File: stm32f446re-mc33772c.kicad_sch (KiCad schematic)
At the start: 44 parts, among them J1 Conn_01x02, J2 USB_B_Micro, J3 Conn_01x03, J4 Conn_01x06, J6 SM06B-GHS-TB, U1 STM32F446RETx, U3 LD1086D2M33TR, U4 AMS1117-3.3, U6 LMR51450SDRRR, U7 SN65HVD232, Y1 16MHz

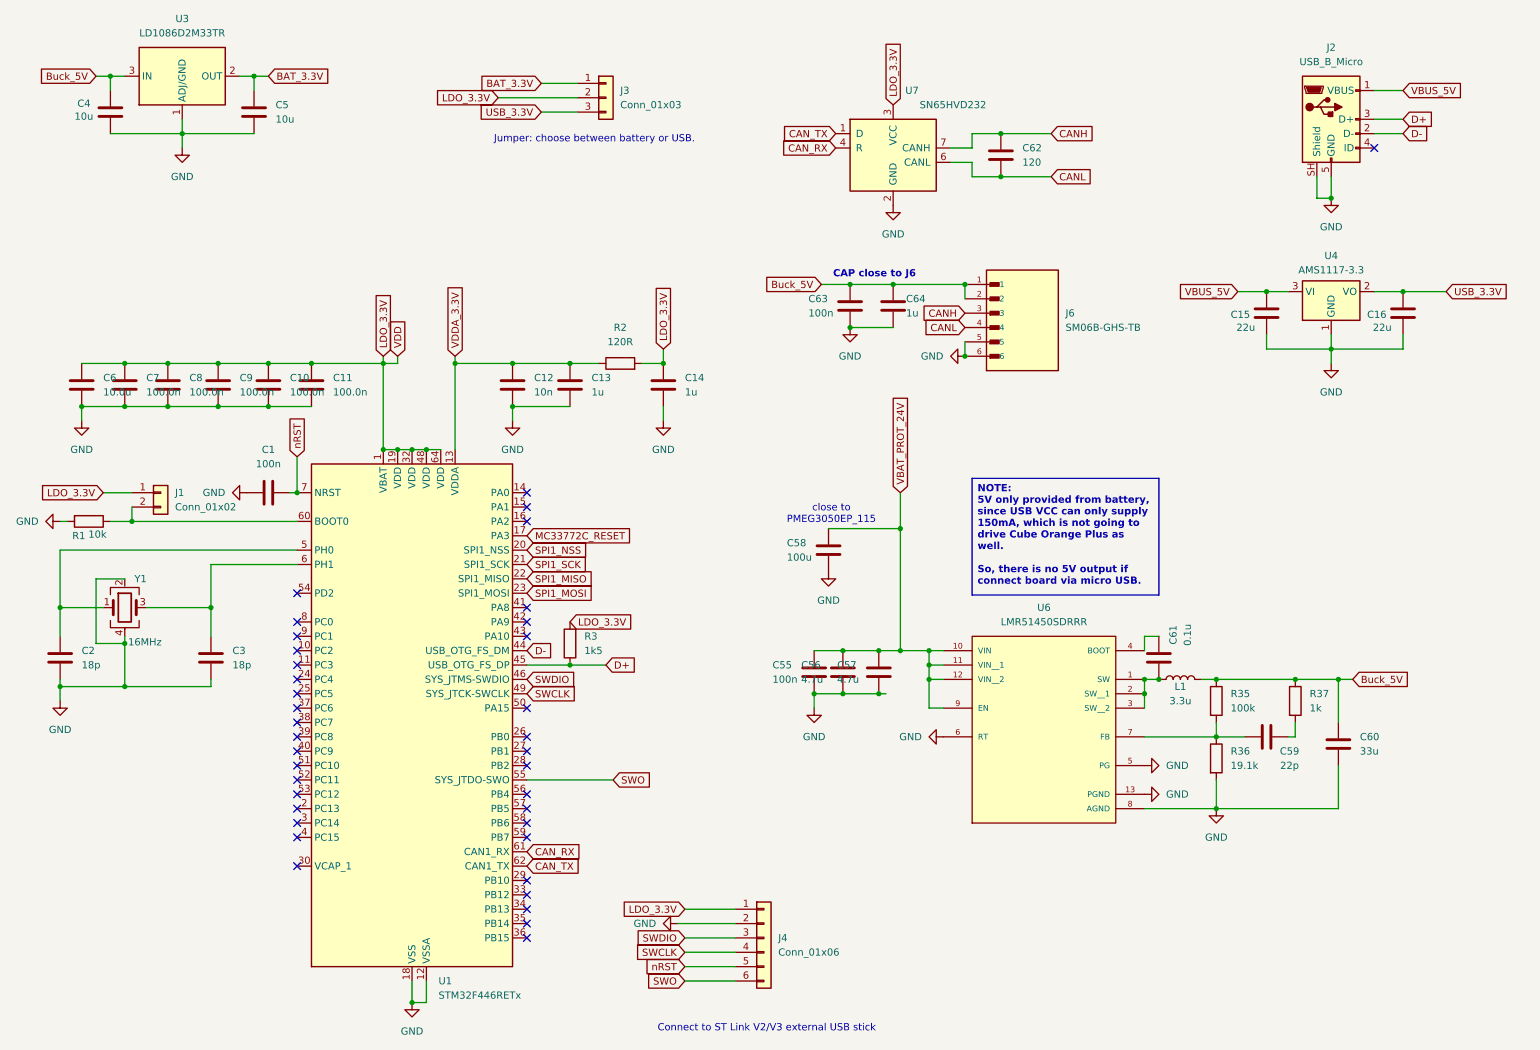
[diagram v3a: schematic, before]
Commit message: fullup the annotation for update PCB from Schematics
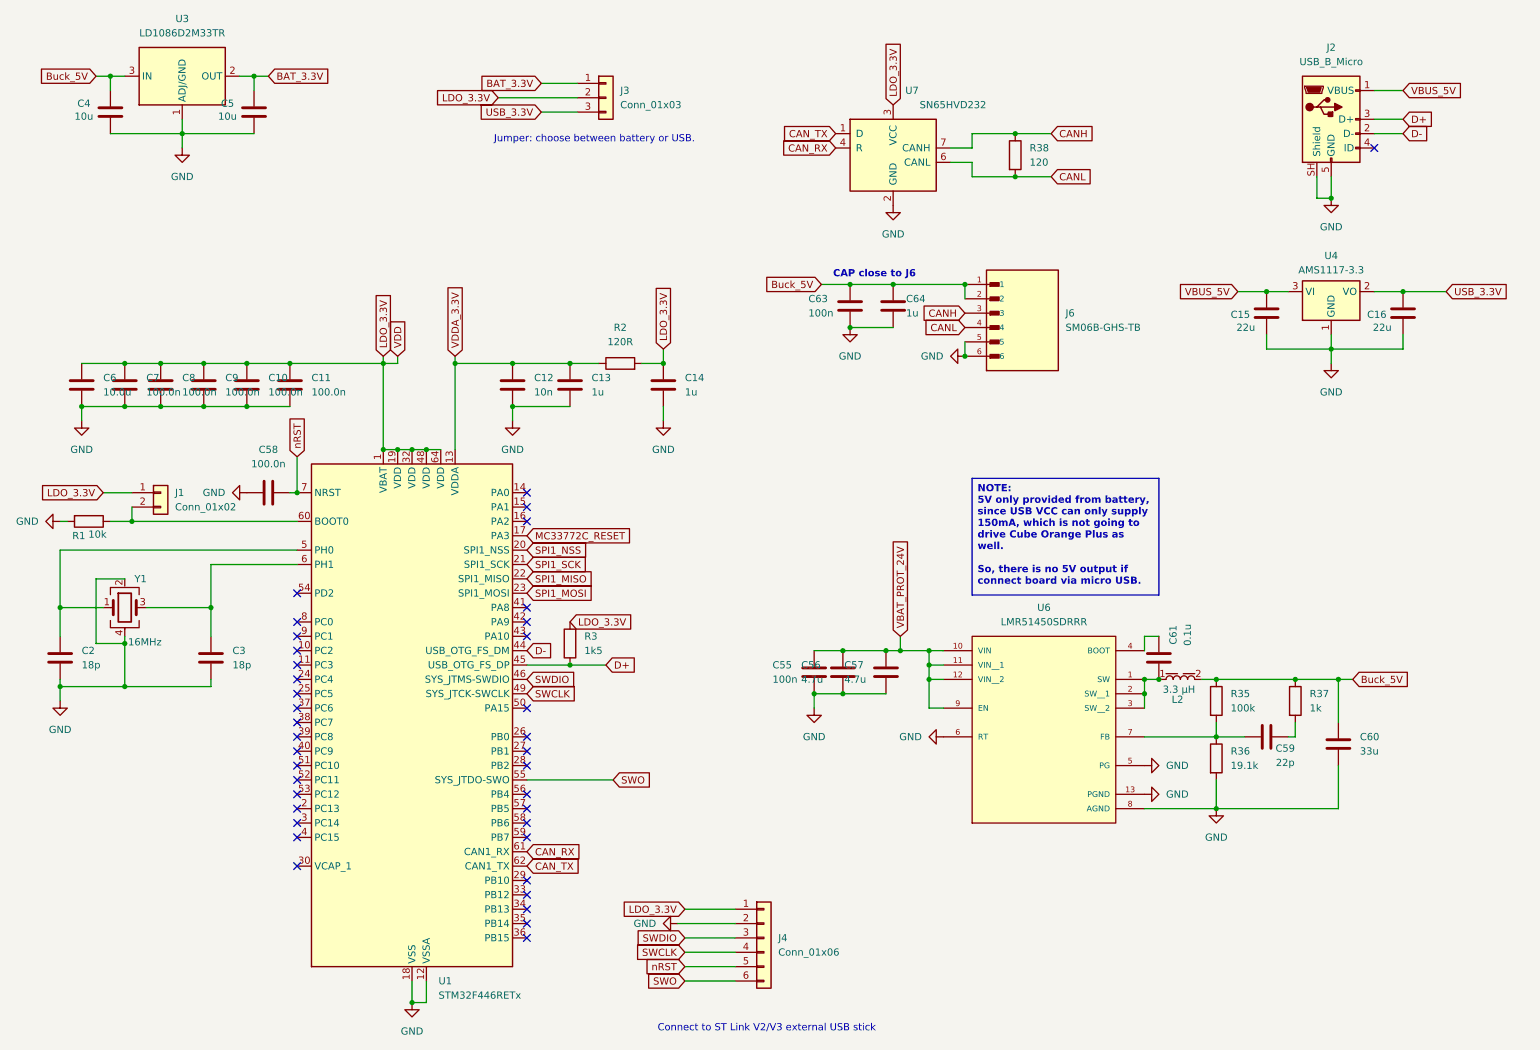
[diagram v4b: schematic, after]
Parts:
- removed C1: 100n, Capacitor_SMD:C_0402_1005Metric, symbol Device:C
- removed C62: 120, symbol Device:C
- removed L1: 3.3u, symbol Device:L
- added L2: 1040_74437368033, Inductor_SMD_Wurth:L_Wurth_WE-LHMI-1040, symbol MyySym:1040_74437368033
- added R38: 120, Resistor_SMD:R_1206_3216Metric, symbol Device:R
- C10, C11, C12, C13, C14, C7, C8, C9: footprint (none) -> Capacitor_SMD:C_0603_1608Metric
- C4, C5, C6: footprint (none) -> Capacitor_SMD:C_0805_2012Metric
- C56, C57: footprint Capacitor_SMD:C_1210_3225Metric -> Capacitor_SMD:C_0805_2012Metric
- C58: value 100u -> 100.0n; footprint (none) -> Capacitor_SMD:C_0603_1608Metric
- C59, C61: footprint (none) -> Capacitor_SMD:C_0402_1005Metric
- C60: footprint (none) -> Capacitor_SMD:C_1206_3216Metric
- J2: footprint (none) -> Connector_USB:USB_Micro-B_Molex-105017-0001
- J3: footprint (none) -> Connector_PinHeader_2.54mm:PinHeader_1x03_P2.54mm_Vertical
- J4: footprint (none) -> Connector_PinHeader_2.54mm:PinHeader_1x06_P2.54mm_Vertical
- J6: footprint SM06B-GHS-TB:JST_SM06B-GHS-TB -> MyFootLib:JST_SM06B-GHS-TB
- R2: footprint Resistor_SMD:R_0805_2012Metric -> Resistor_SMD:R_0603_1608Metric
- R35, R36, R37: footprint (none) -> Resistor_SMD:R_0402_1005Metric
- U6: footprint LMR51450SDRRR:CONV_LMR51450SDRRR -> MyFootLib:LMR51450SDRRR
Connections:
- net Buck_5V: now also L2.2
- net CANH: now also R38.1
- net CANL: now also R38.2
- net GND: now also C58.1; no longer C58.2
- net VBAT_PROT_24V: no longer C58.1
- net nRST: now also C58.2
- net at C61.2, U6.1 (SW), U6.2 (SW__1)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: now also L2.1
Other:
- note removed: "close to PMEG3050EP_115"

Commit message: update annotation
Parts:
- L2: footprint Inductor_SMD_Wurth:L_Wurth_WE-LHMI-1040 -> MyFootLib:L_Wurth_WE-LHMI-1040
- R1: footprint (none) -> Resistor_SMD:R_0402_1005Metric
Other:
- moved on the sheet: C15, C16, U4
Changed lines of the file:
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@@
 		)
 	)
-	(text_box "NOTE:\n5V only provided from battery, since USB VCC can only supply 150mA, which is not going to drive Cube Orange Plus as well.\n\nSo, there is no 5V output if connect board via micro USB."
+	(text_box "NOTE:\n5V only provided from battery, since USB VCC can only supply 150mA, which is not going to drive Cube Orange Plus as well.\n\nSo, there is no 5V output if we connect board via micro USB."
 		(exclude_from_sim no)
 		(at 185.42 95.25 0)
@@
 	)
 	(junction
-		(at 237.49 62.23)
+		(at 243.84 62.23)
 		(diameter 0)
 		(color 0 0 0 0)
@@
 	)
 	(junction
-		(at 261.62 62.23)
-		(diameter 0)
-		(color 0 0 0 0)
-	)
-	(junction
 		(at 163.83 68.58)
 		(diameter 0)
@@
 	)
 	(junction
+		(at 267.97 62.23)
+		(diameter 0)
+		(color 0 0 0 0)
+	)
+	(junction
 		(at 41.91 74.93)
 		(diameter 0)
@@
 	)
 	(junction
-		(at 248.92 72.39)
+		(at 255.27 72.39)
 		(diameter 0)
 		(color 0 0 0 0)
@@
 	(wire
 		(pts
-			(xy 261.62 69.85) (xy 261.62 72.39)
+			(xy 267.97 69.85) (xy 267.97 72.39)
 		)
 		(stroke
@@
 	(wire
 		(pts
-			(xy 237.49 62.23) (xy 241.3 62.23)
+			(xy 243.84 62.23) (xy 247.65 62.23)
 		)
 		(stroke
@@
 	(wire
 		(pts
-			(xy 237.49 72.39) (xy 237.49 69.85)
+			(xy 243.84 72.39) (xy 243.84 69.85)
 		)
 		(stroke
@@
 	(wire
 		(pts
-			(xy 248.92 69.85) (xy 248.92 72.39)
+			(xy 255.27 69.85) (xy 255.27 72.39)
 		)
 		(stroke
@@
 	(wire
 		(pts
-			(xy 248.92 72.39) (xy 248.92 74.93)
+			(xy 255.27 72.39) (xy 255.27 74.93)
 		)
 		(stroke
@@
 	(wire
 		(pts
-			(xy 248.92 72.39) (xy 237.49 72.39)
+			(xy 255.27 72.39) (xy 243.84 72.39)
 		)
 		(stroke
@@
 	(wire
 		(pts
-			(xy 232.41 62.23) (xy 237.49 62.23)
+			(xy 238.76 62.23) (xy 243.84 62.23)
 		)
 		(stroke
@@
 	(wire
 		(pts
-			(xy 261.62 62.23) (xy 269.24 62.23)
+			(xy 267.97 62.23) (xy 270.51 62.23)
 		)
 		(stroke
@@
 	(wire
 		(pts
-			(xy 256.54 62.23) (xy 261.62 62.23)
+			(xy 262.89 62.23) (xy 267.97 62.23)
 		)
 		(stroke
@@
 	(wire
 		(pts
-			(xy 261.62 72.39) (xy 248.92 72.39)
+			(xy 267.97 72.39) (xy 255.27 72.39)
 		)
 		(stroke
@@
 	(global_label "USB_3.3V"
 		(shape input)
-		(at 269.24 62.23 0)
+		(at 270.51 62.23 0)
 		(fields_autoplaced yes)
 		(effects
@@
 		)
 		(property "Intersheetrefs" "${INTERSHEET_REFS}"
-			(at 281.1152 62.23 0)
+			(at 282.3852 62.23 0)
 			(hide yes)
 			(show_name no)
@@
 	(global_label "VBUS_5V"
 		(shape input)
-		(at 232.41 62.23 180)
+		(at 238.76 62.23 180)
 		(fields_autoplaced yes)
 		(effects
@@
 		)
 		(property "Intersheetrefs" "${INTERSHEET_REFS}"
-			(at 221.2605 62.23 0)
+			(at 227.6105 62.23 0)
 			(hide yes)
 			(show_name no)
@@
 			)
 		)
-		(property "Footprint" ""
+		(property "Footprint" "Resistor_SMD:R_0402_1005Metric"
 			(at 29.21 101.092 90)
 			(hide yes)
@@
 	(symbol
 		(lib_id "Device:C")
-		(at 261.62 66.04 0)
+		(at 267.97 66.04 0)
 		(unit 1)
 		(body_style 1)
@@
 		(dnp no)
 		(property "Reference" "C16"
-			(at 255.27 66.294 0)
+			(at 261.62 66.294 0)
 			(show_name no)
 			(do_not_autoplace no)
@@
 		)
 		(property "Value" "22u"
-			(at 256.286 68.58 0)
+			(at 262.636 68.58 0)
 			(show_name no)
 			(do_not_autoplace no)
@@
 		)
 		(property "Footprint" "Capacitor_SMD:C_0402_1005Metric"
-			(at 262.5852 69.85 0)
+			(at 268.9352 69.85 0)
 			(hide yes)
 			(show_name no)
@@
 		)
 		(property "Datasheet" ""
-			(at 261.62 66.04 0)
+			(at 267.97 66.04 0)
 			(hide yes)
 			(show_name no)
@@
 		)
 		(property "Description" "Unpolarized capacitor"
-			(at 261.62 66.04 0)
+			(at 267.97 66.04 0)
 			(hide yes)
 			(show_name no)
@@
 	(symbol
 		(lib_id "Device:C")
-		(at 237.49 66.04 0)
+		(at 243.84 66.04 0)
 		(unit 1)
 		(body_style 1)
@@
 		(dnp no)
 		(property "Reference" "C15"
-			(at 231.14 66.294 0)
+			(at 237.49 66.294 0)
 			(show_name no)
 			(do_not_autoplace no)
@@
 		)
 		(property "Value" "22u"
-			(at 232.156 68.58 0)
+			(at 238.506 68.58 0)
 			(show_name no)
 			(do_not_autoplace no)
@@
 		)
 		(property "Footprint" "Capacitor_SMD:C_0402_1005Metric"
-			(at 238.4552 69.85 0)
+			(at 244.8052 69.85 0)
 			(hide yes)
 			(show_name no)
@@
 		)
 		(property "Datasheet" ""
-			(at 237.49 66.04 0)
+			(at 243.84 66.04 0)
 			(hide yes)
 			(show_name no)
@@
 		)
 		(property "Description" "Unpolarized capacitor"
-			(at 237.49 66.04 0)
+			(at 243.84 66.04 0)
 			(hide yes)
 			(show_name no)
@@
 	(symbol
 		(lib_id "Regulator_Linear:AMS1117-3.3")
-		(at 248.92 62.23 0)
+		(at 255.27 62.23 0)
 		(unit 1)
 		(body_style 1)
@@
 		(fields_autoplaced yes)
 		(property "Reference" "U4"
-			(at 248.92 55.88 0)
+			(at 255.27 55.88 0)
 			(show_name no)
 			(do_not_autoplace no)
@@
 		)
 		(property "Value" "AMS1117-3.3"
-			(at 248.92 58.42 0)
+			(at 255.27 58.42 0)
 			(show_name no)
 			(do_not_autoplace no)
@@
 		)
 		(property "Footprint" "Package_TO_SOT_SMD:SOT-223-3_TabPin2"
-			(at 248.92 57.15 0)
+			(at 255.27 57.15 0)
 			(hide yes)
 			(show_name no)
@@
 		)
 		(property "Datasheet" "http://www.advanced-monolithic.com/pdf/ds1117.pdf"
-			(at 251.46 68.58 0)
+			(at 257.81 68.58 0)
 			(hide yes)
 			(show_name no)
@@
 		)
 		(property "Description" "1A Low Dropout regulator, positive, 3.3V fixed output, SOT-223"
-			(at 248.92 62.23 0)
+			(at 255.27 62.23 0)
 			(hide yes)
 			(show_name no)
@@
 			)
 		)
-		(property "Footprint" "Inductor_SMD_Wurth:L_Wurth_WE-LHMI-1040"
+		(property "Footprint" "MyFootLib:L_Wurth_WE-LHMI-1040"
 			(at 222.25 123.19 0)
 			(hide yes)
@@
 	(symbol
 		(lib_id "power:GND")
-		(at 248.92 74.93 0)
+		(at 255.27 74.93 0)
 		(unit 1)
 		(body_style 1)
@@
 		(fields_autoplaced yes)
 		(property "Reference" "#PWR010"
-			(at 248.92 81.28 0)
+			(at 255.27 81.28 0)
 			(hide yes)
 			(show_name no)
@@
 		)
 		(property "Value" "GND"
-			(at 248.92 80.01 0)
+			(at 255.27 80.01 0)
 			(show_name no)
 			(do_not_autoplace no)
@@
 		)
 		(property "Footprint" ""
-			(at 248.92 74.93 0)
+			(at 255.27 74.93 0)
 			(hide yes)
 			(show_name no)
@@
 		)
 		(property "Datasheet" ""
-			(at 248.92 74.93 0)
+			(at 255.27 74.93 0)
 			(hide yes)
 			(show_name no)
@@
 		)
 		(property "Description" "Power symbol creates a global label with name \"GND\" , ground"
-			(at 248.92 74.93 0)
+			(at 255.27 74.93 0)
 			(hide yes)
 			(show_name no)

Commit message: good placement
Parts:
- removed J4: Conn_01x06, Connector_PinHeader_2.54mm:PinHeader_1x06_P2.54mm_Vertical, symbol Connector_Generic:Conn_01x06
- added J4: Conn_01x03, Connector_PinHeader_1.00mm:PinHeader_1x03_P1.00mm_Vertical, symbol Connector_Generic:Conn_01x03
- J3: footprint Connector_PinHeader_2.54mm:PinHeader_1x03_P2.54mm_Vertical -> Connector_PinHeader_1.00mm:PinHeader_1x03_P1.00mm_Vertical
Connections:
- net BAT_3.3V: now also J4.1 (Pin_1); no longer J3.1 (Pin_1)
- net GND: now also J3.1 (Pin_1)
- net LDO_3.3V: now also J4.2 (Pin_2); no longer J3.2 (Pin_2)
- net SWCLK: now also J3.3 (Pin_3)
- net SWDIO: now also J3.2 (Pin_2)
- net USB_3.3V: now also J4.3 (Pin_3); no longer J3.3 (Pin_3)
- net SWO: no longer names the net of U1.55 (PB3)
- no-connect marks 38 -> 39
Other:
- note removed: "Connect to ST Link V2/V3 external USB stick"

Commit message: GND, power_flag
1. F.Cu and B.Cu fill zone with GND
2. add power_flag
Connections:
- net BAT_3.3V renamed BAT_3V3
- net LDO_3.3V renamed LDO_3V3
- net USB_3.3V renamed USB_3V3
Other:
- moved on the sheet: C4, C5, J4, U3
